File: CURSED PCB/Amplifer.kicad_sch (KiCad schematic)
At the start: 11 parts, among them U1 MCP3562-E_ST, U2 OPA196xDBV, U3 MCP1501-30xSN

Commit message: Added some amplifer stuff
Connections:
- net anti-aliasing filter/VIN: now reaches U2.1
- net anti-aliasing filter/VIN: no longer U1.5 (CH0)
- net SCK renamed SCLK
- new net anti-aliasing filter/VOUT: U1.5 (CH0)
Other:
- added sheet anti-aliasing filter (Filter.kicad_sch)
- moved on the sheet: U1

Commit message: Updates to PCB before exam sesaon
idk what I added ngl
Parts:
- removed C5: C_Small, symbol Device:C_Small
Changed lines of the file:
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@@
-	)
-	(symbol
-		(lib_id "Device:C_Small")
-		(at 115.57 109.22 0)
-		(unit 1)
-		(exclude_from_sim no)
-		(in_bom yes)
-		(on_board yes)
-		(dnp no)
-		(property "Reference" "C5"
-			(at 118.11 107.9562 0)
-			(effects
-				(font
-					(size 1.27 1.27)
-				)
-				(justify left)
-			)
-		)
-		(property "Value" "C_Small"
-			(at 118.11 110.4962 0)
-			(effects
-				(font
-					(size 1.27 1.27)
-				)
-				(justify left)
-			)
-		)
-		(property "Footprint" ""
-			(at 115.57 109.22 0)
-			(effects
-				(font
-					(size 1.27 1.27)
-				)
-				(hide yes)
-			)
-		)
-		(property "Datasheet" "~"
-			(at 115.57 109.22 0)
-			(effects
-				(font
-					(size 1.27 1.27)
-				)
-				(hide yes)
-			)
-		)
-		(property "Description" "Unpolarized capacitor, small symbol"
-			(at 115.57 109.22 0)
-			(effects
-				(font
-					(size 1.27 1.27)
-				)
-				(hide yes)
-			)
-		)
-		(pin "1"
-		)
-		(pin "2"
-		)
-		(instances
-			(project "sensor_1"
-				(path "/9fb1a86f-679c-4b88-9ed1-932f4f414580/543706d6-8cb0-4c51-81f6-888765ec3907"
-					(reference "C5")
-					(unit 1)
-				)
-			)
-		)
 	)
 	(symbol

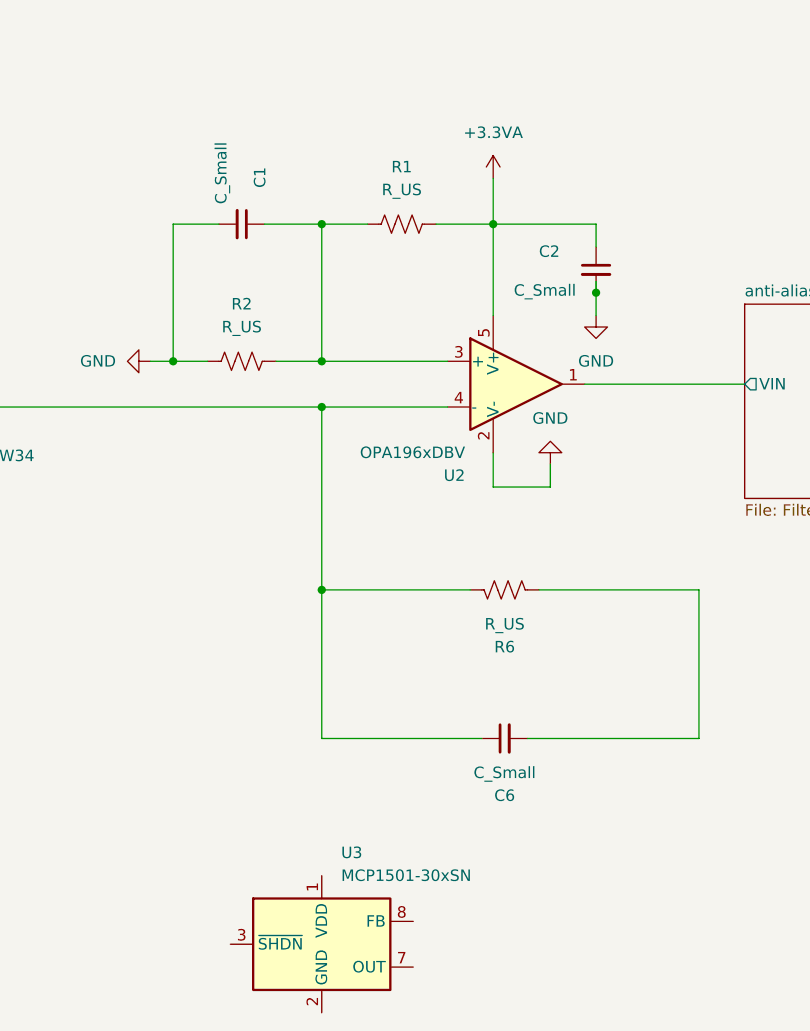
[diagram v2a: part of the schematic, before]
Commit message: Added values for schematic
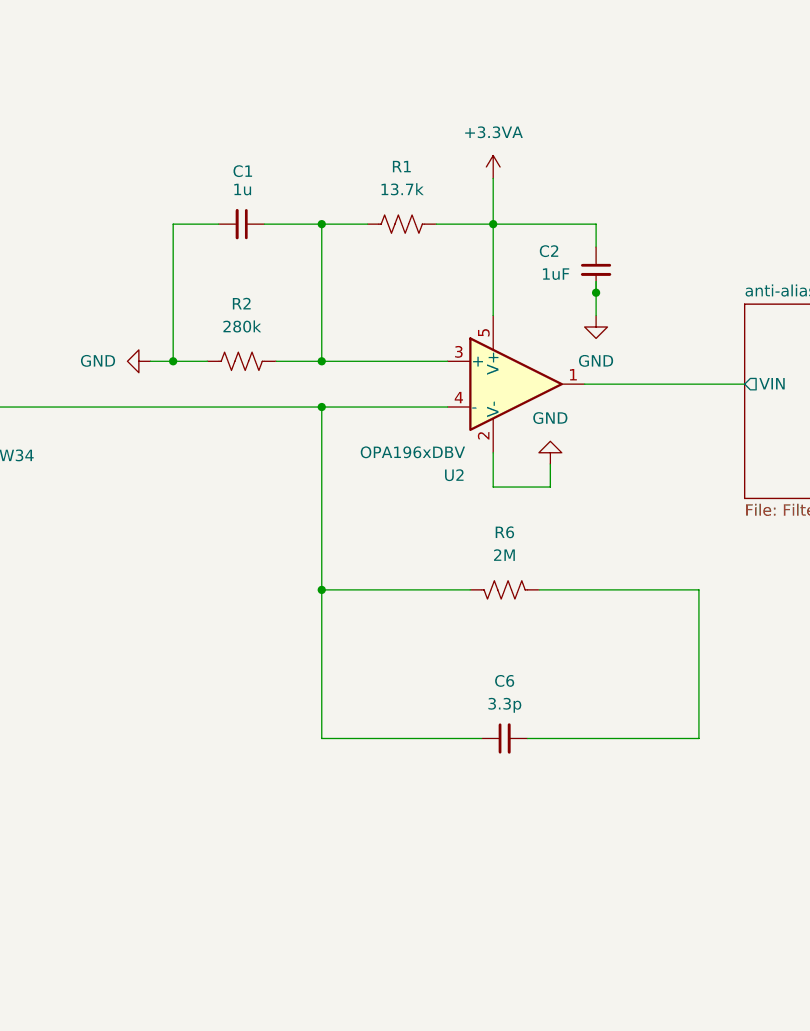
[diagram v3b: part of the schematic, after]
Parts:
- removed U3: MCP1501-30xSN, Package_SO:SOIC-8_3.9x4.9mm_P1.27mm, symbol Reference_Voltage:MCP1501-30xSN
- C1: value C_Small -> 1u
- C2: value C_Small -> 1uF
- C6: value C_Small -> 3.3p
- R1: value R_US -> 13.7k
- R2: value R_US -> 280k
- R6: value R_US -> 2M
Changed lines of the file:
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@@
 		(fields_autoplaced yes)
 		(property "Reference" "C6"
-			(at 154.9463 130.81 90)
-			(effects
-				(font
-					(size 1.27 1.27)
-				)
-			)
-		)
-		(property "Value" "C_Small"
-			(at 154.9463 128.27 90)
+			(at 154.9463 118.11 90)
+			(effects
+				(font
+					(size 1.27 1.27)
+				)
+			)
+		)
+		(property "Value" "3.3p"
+			(at 154.9463 120.65 90)
 			(effects
 				(font
@@
 			)
 		)
-		(property "Value" "C_Small"
-			(at 155.956 74.676 0)
+		(property "Value" "1uF"
+			(at 159.004 72.898 0)
 			(effects
 				(font
@@
 			)
 		)
-		(property "Value" "R_US"
+		(property "Value" "13.7k"
 			(at 143.51 63.5 90)
 			(effects
@@
 		(dnp no)
 		(property "Reference" "C1"
-			(at 127.762 60.96 0)
+			(at 124.714 61.468 90)
 			(effects
 				(font
@@
 			)
 		)
-		(property "Value" "C_Small"
-			(at 123.444 58.166 0)
+		(property "Value" "1u"
+			(at 124.714 63.5 90)
 			(effects
 				(font
@@
 		(fields_autoplaced yes)
 		(property "Reference" "R6"
-			(at 154.94 114.3 90)
-			(effects
-				(font
-					(size 1.27 1.27)
-				)
-			)
-		)
-		(property "Value" "R_US"
-			(at 154.94 111.76 90)
+			(at 154.94 101.6 90)
+			(effects
+				(font
+					(size 1.27 1.27)
+				)
+			)
+		)
+		(property "Value" "2M"
+			(at 154.94 104.14 90)
 			(effects
 				(font
@@
 				(path "/9fb1a86f-679c-4b88-9ed1-932f4f414580/543706d6-8cb0-4c51-81f6-888765ec3907"
 					(reference "#PWR04")
-					(unit 1)
-				)
-			)
-		)
-	)
-	(symbol
-		(lib_id "Reference_Voltage:MCP1501-30xSN")
-		(at 134.62 147.32 0)
-		(unit 1)
-		(exclude_from_sim no)
-		(in_bom yes)
-		(on_board yes)
-		(dnp no)
-		(fields_autoplaced yes)
-		(property "Reference" "U3"
-			(at 136.7633 137.16 0)
-			(effects
-				(font
-					(size 1.27 1.27)
-				)
-				(justify left)
-			)
-		)
-		(property "Value" "MCP1501-30xSN"
-			(at 136.7633 139.7 0)
-			(effects
-				(font
-					(size 1.27 1.27)
-				)
-				(justify left)
-			)
-		)
-		(property "Footprint" "Package_SO:SOIC-8_3.9x4.9mm_P1.27mm"
-			(at 134.62 147.32 0)
-			(effects
-				(font
-					(size 1.27 1.27)
-				)
-				(hide yes)
-			)
-		)
-		(property "Datasheet" "http://ww1.microchip.com/downloads/en/DeviceDoc/20005474E.pdf"
-			(at 139.7 147.32 0)
-			(effects
-				(font
-					(size 1.27 1.27)
-				)
-				(hide yes)
-			)
-		)
-		(property "Description" "3V, 0.1%, 20mA, Precision Voltage Reference, SOIC-8"
-			(at 134.62 147.32 0)
-			(effects
-				(font
-					(size 1.27 1.27)
-				)
-				(hide yes)
-			)
-		)
-		(pin "8"
-		)
-		(pin "2"
-		)
-		(pin "7"
-		)
-		(pin "3"
-		)
-		(pin "4"
-		)
-		(pin "1"
-		)
-		(pin "5"
-		)
-		(pin "6"
-		)
-		(instances
-			(project ""
-				(path "/9fb1a86f-679c-4b88-9ed1-932f4f414580/543706d6-8cb0-4c51-81f6-888765ec3907"
-					(reference "U3")
 					(unit 1)
 				)
@@
 			)
 		)
-		(property "Value" "R_US"
+		(property "Value" "280k"
 			(at 125.73 78.74 90)
 			(effects

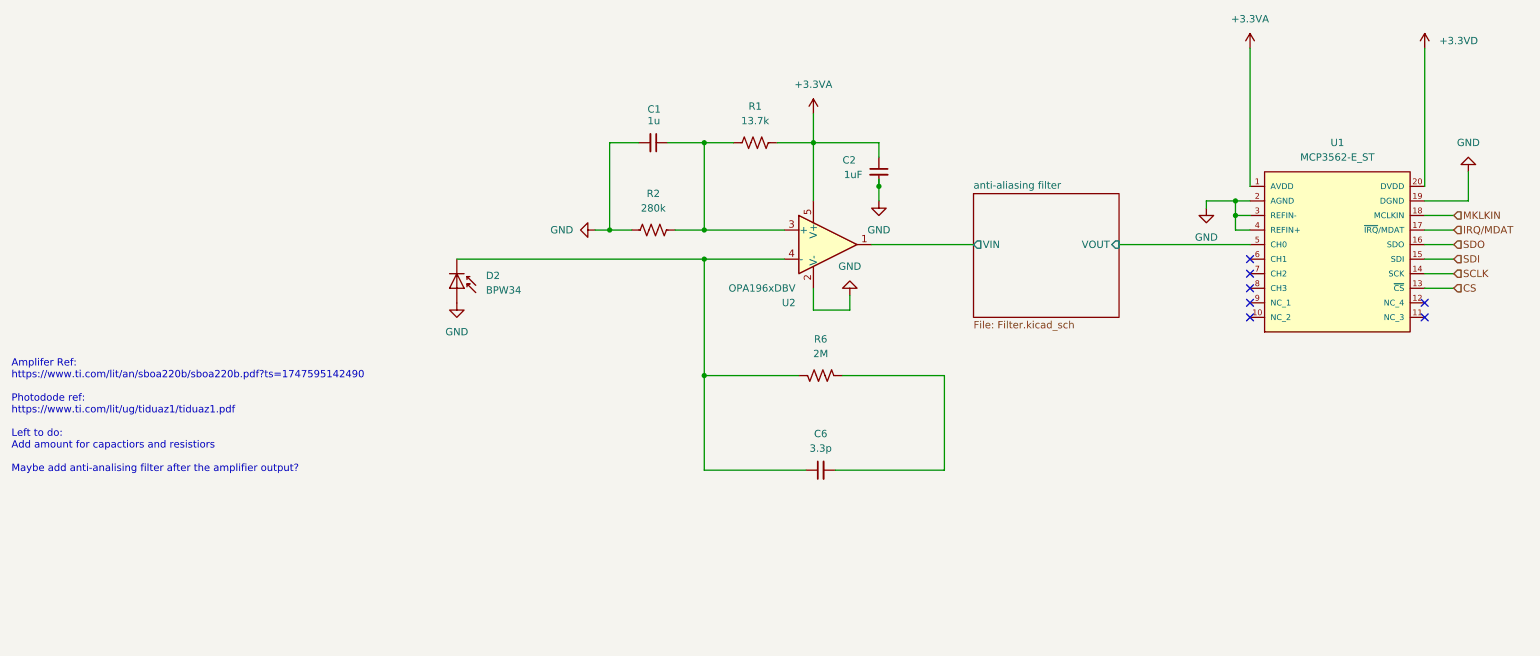
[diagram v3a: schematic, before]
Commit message: Added reference voltage and some other stuff
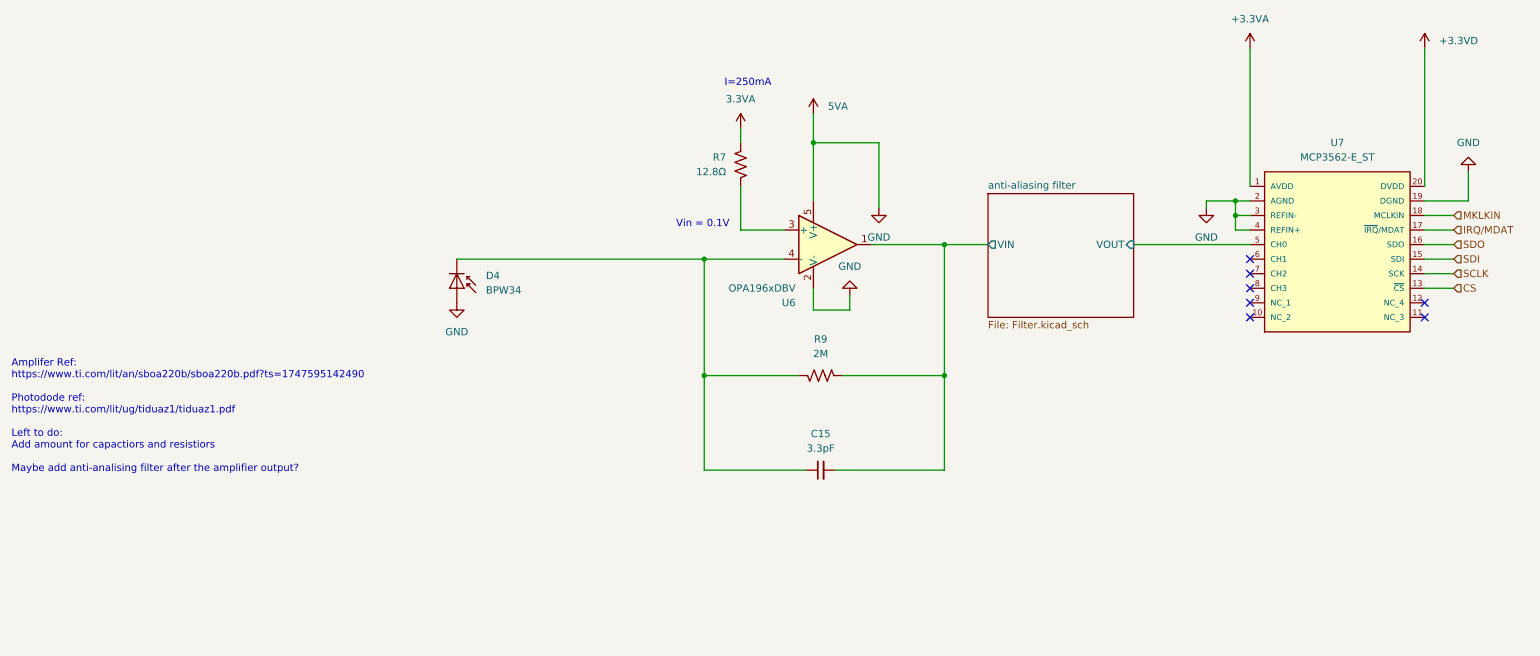
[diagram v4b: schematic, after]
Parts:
- removed C1: 1u, symbol Device:C_Small
- removed C2: 1uF, symbol Device:C_Small
- removed R1: 13.7k, symbol Device:R_US
- removed R2: 280k, symbol Device:R_US
- added R7: 12.8Ω, Resistor_SMD:R_0201_0603Metric, symbol Device:R_US
- C15: renamed from C6; value 3.3p -> 3.3pF; footprint (none) -> Capacitor_SMD:C_0201_0603Metric_Pad0.64x0.40mm_HandSolder
- R9: renamed from R6; footprint (none) -> Resistor_SMD:R_0201_0603Metric
- U7: renamed from U1; footprint MCP3562-E_ST:TSSOP-20_MICROCHIP_TECHNOLOGY -> canhw_footprints:TSSOP20_ST_MCH
- renumbered D2 to D4, U2 to U6
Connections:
- net +3.3VA: no longer U6.5 (V+)
- net anti-aliasing filter/VIN: now also C15.2, R9.2
- net at U6.3 (+): now also R7.1
- net GND renamed 5VA
- net 5VA: now also U6.5 (V+)
- new net 3.3VA: R7.2
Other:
- note added: "I=250mA"
- note added: "Vin = 0.1V"

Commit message: Fixes to schematic
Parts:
- added C14: 1u, symbol Device:C
- added R8: 13.7k, symbol Device:R_US
- R7: value 12.8Ω -> 280; footprint Resistor_SMD:R_0201_0603Metric -> (none)
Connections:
- net 3.3VA is gone; now on net 5VA: R7.2
- net 5VA: now also C14.1, R8.1; no longer D4.2 (A), U6.2 (V-), U7.19 (DGND), U7.2 (AGND), U7.3 (REFIN-), U7.4 (REFIN+)
- net at R7.1, U6.3 (+): now also C14.2, R8.2
- new net GND: D4.2 (A), U6.2 (V-), U7.19 (DGND), U7.2 (AGND), U7.3 (REFIN-), U7.4 (REFIN+)
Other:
- note removed: "I=250mA"
- note removed: "Vin = 0.1V"
